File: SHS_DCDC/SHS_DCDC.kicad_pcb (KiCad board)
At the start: 6 copper layers, 100 x 100 mm, 130 parts, among them J1 Barrel_Jack, J2 USB_A, J3 Conn_ARM_JTAG_SWD_10, J4 Conn_01x02_Male, Q1 BSS84, Q10 PMV100XPEAR, Q11 PMV100XPEAR, Q12 PMV100XPEAR, Q13 PMV100XPEAR, Q14 PMV100XPEAR, Q15 BSS84, Q16 PMV100XPEAR, Q17 PMV100XPEAR, Q18 BSS84, Q19 2N7002, Q2 PMV100XPEAR, Q20 BSS84, Q21 2N7002, Q3 2N7002, Q4 2N7002, Q5 PMV100XPEAR, Q6 2N7002, Q7 PMV100XPEAR, Q8 Q_PMOS_DGS, Q9 PMV100XPEAR, U1 RT8299-WDFN10L, U2 INA181, U3 LMV324AIDR, U4 LMV358IDR, U5 MP3414A, U6 ESP32-S2-MINI-1, U7 MCP101, U8 MIC5501-3.0YM5, U9 BD49LxxG, Y1 2-SMD no lead

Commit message: 3D rendering progress
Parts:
- removed S1: TS02-66-70-BK-160-LCR-D, Library:SW_TS02-66-70-BK-160-LCR-D
- added SW1: TACT_SW, SHS_DCDC:ESWITCH_TL1105, B.Cu at (7.60, 58.9)
- J1, J2: moved to B.Cu
- L2: value L -> 1.5 uH
- moved C26 8.01 mm to (83.5, 19.4), turned to 0 degrees
- moved C27 8.00 mm to (83.5, 15.8), turned to 0 degrees
- moved J2 5.00 mm to (85.0, 12.0), turned to 0 degrees
- turned J1 to -90 degrees
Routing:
- net Net-(L2-Pad1): track 9.46 -> 0.00 mm
- net USB_D-: track 99.9 -> 107.8 mm
- net Net-(C26-Pad2): track 60.0 -> 55.8 mm
- net USB_D+: track 97.2 -> 98.9 mm

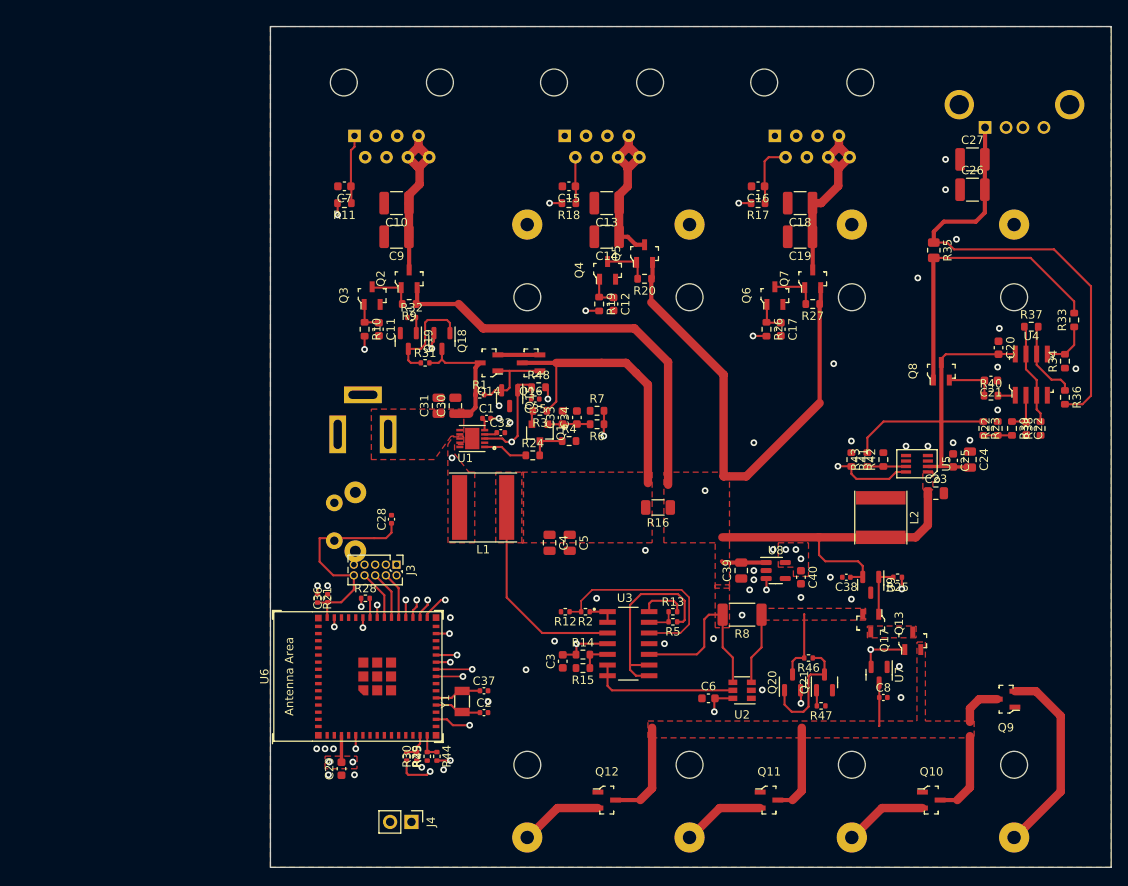
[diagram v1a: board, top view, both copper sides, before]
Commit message: 3D missing part
Many parts with no 3D view, have completed all of them
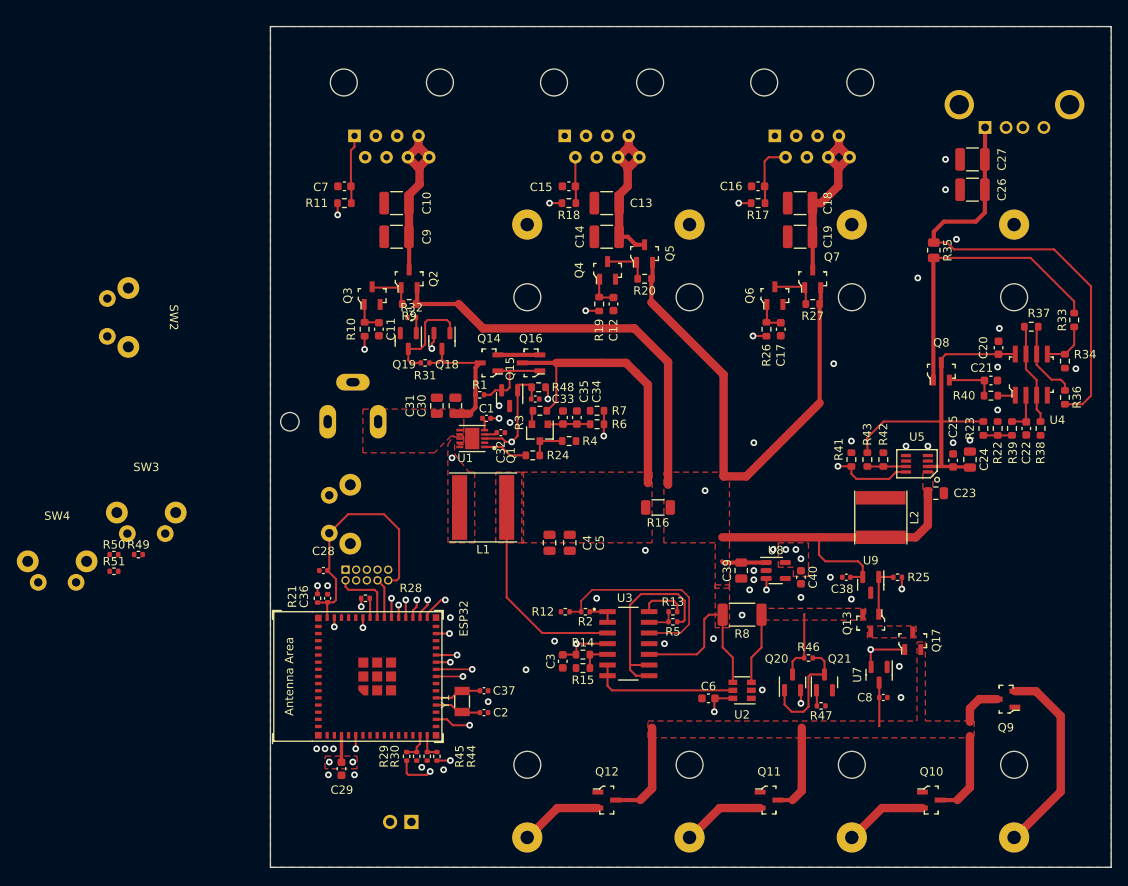
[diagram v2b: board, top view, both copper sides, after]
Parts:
- added R49: 10k, Resistor_SMD:R_0402_1005Metric, F.Cu at (-15.7, 62.8)
- added R50: 10k, Resistor_SMD:R_0402_1005Metric, F.Cu at (-18.6, 62.8)
- added R51: 10k, Resistor_SMD:R_0402_1005Metric, F.Cu at (-18.6, 64.8)
- added SW2: TACT_SW, SHS_DCDC:ESWITCH_TL1105, F.Cu at (-19.4, 34.6)
- added SW3: TACT_SW, SHS_DCDC:ESWITCH_TL1105, F.Cu at (-14.8, 60.3)
- added SW4: TACT_SW, SHS_DCDC:ESWITCH_TL1105, F.Cu at (-25.4, 66.1)
- J1: value Barrel_Jack -> PJ-059A; footprint digikey-footprints:Barrel_Jack_5.5mmODx2.1mmID_PJ-202A -> SHS_DCDC:CUI_PJ-059A
- J3, J4: moved to B.Cu
- moved C28 10.1 mm to (6.30, 64.7), turned to 180 degrees
- moved J3 6.10 mm to (8.93, 64.6)
- moved J1 2.35 mm to (12.8, 47.0), turned to 180 degrees
- moved SW1 1.08 mm to (7.00, 58.0)
- moved C31 0.20 mm to (19.8, 45.1)
- turned J4 to 90 degrees
- renumbered U6 to ESP32
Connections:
- J1 pad 3: (no net) -> GND
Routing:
- net MCU_TL_ONOFFSIG: track 71.7 -> 14.1 mm
- net V_MCU: track 115.2 -> 83.4 mm
- net MCU_RST: track 26.0 -> 29.8 mm
- net MCU_MTCK: track 5.66 -> 7.76 mm, vias 0 -> 1
- net MCU_MTMS: track 5.98 -> 7.81 mm, vias 1 -> 0
- net MCU_MTDI: track 6.01 -> 4.77 mm
- net MCU_MTDO: track 5.83 -> 6.11 mm, vias 0 -> 1

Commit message: ESP32 cornering
Moving the ESP32 on the bottom corner of the board
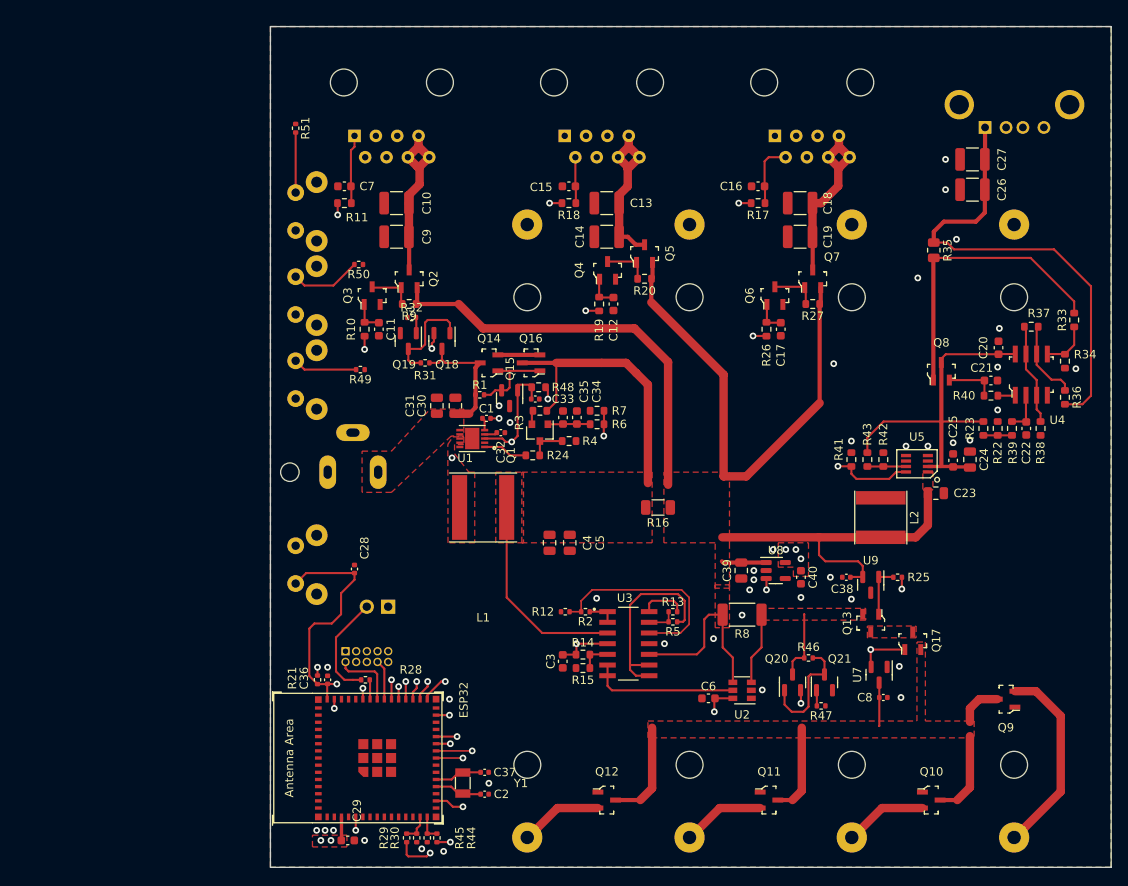
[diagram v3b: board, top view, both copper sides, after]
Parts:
- SW2, SW3, SW4: moved to B.Cu
- moved R51 57.0 mm to (3.00, 12.1), turned to -90 degrees
- moved SW4 52.4 mm to (3.00, 22.0), turned to 90 degrees
- moved R50 45.1 mm to (10.5, 28.3), turned to 180 degrees
- moved R49 34.4 mm to (10.7, 40.8), turned to 180 degrees
- moved SW3 33.4 mm to (3.00, 32.0), turned to 90 degrees
- moved J4 25.7 mm to (14.0, 69.0)
- moved SW2 23.6 mm to (3.00, 42.0), turned to 90 degrees
- moved C2 9.70 mm to (25.5, 91.3)
- moved C37 9.70 mm to (25.5, 88.7)
- moved Y1 9.70 mm to (22.9, 90.0)
- moved C36 9.70 mm to (6.80, 77.7)
- moved ESP32 9.70 mm to (12.7, 87.0)
- moved J3 9.70 mm to (8.93, 74.3)
- moved R21 9.70 mm to (5.60, 77.7)
- moved R28 9.70 mm to (11.3, 77.7)
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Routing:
- net MCU_5V_EN: track 70.4 -> 24.7 mm
- net MCU_BL1_ONOFFSIG: track 74.5 -> 57.3 mm
- net MCU_TX: track 28.5 -> 12.6 mm, vias 1 -> 0
- net USB_D-: track 107.8 -> 118.9 mm
- net MCU_RX: track 26.7 -> 17.0 mm
- net MCU_PWM_BL2: track 70.8 -> 80.5 mm
- net Net-(Q18-Pad2): track 57.0 -> 66.7 mm
- net MCU_PWM_TL: track 35.4 -> 45.1 mm
- net MCU_PWM_BL1: track 53.9 -> 63.6 mm
- net MCU_CTRL_B2: track 0.00 -> 8.46 mm
- net MCU_BL2_ONOFFSIG: track 89.1 -> 97.2 mm
- net MCU_CTRL_B1: track 0.00 -> 7.62 mm
- net USB_D+: track 98.9 -> 106.2 mm
- net MCU_CTRL_B3: track 0.00 -> 7.15 mm
- net MCU_RST: track 29.8 -> 35.9 mm, vias 0 -> 1
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- added copper zone on B.Cu, net GND

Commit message: DFU update
PCB update to setup 3 ways of FW/Debug capability:
1. JTAG (FW & Debug)
2. USB DFU (FW & Debug)
3. UART (FW only)
With BOOT0 button installed too
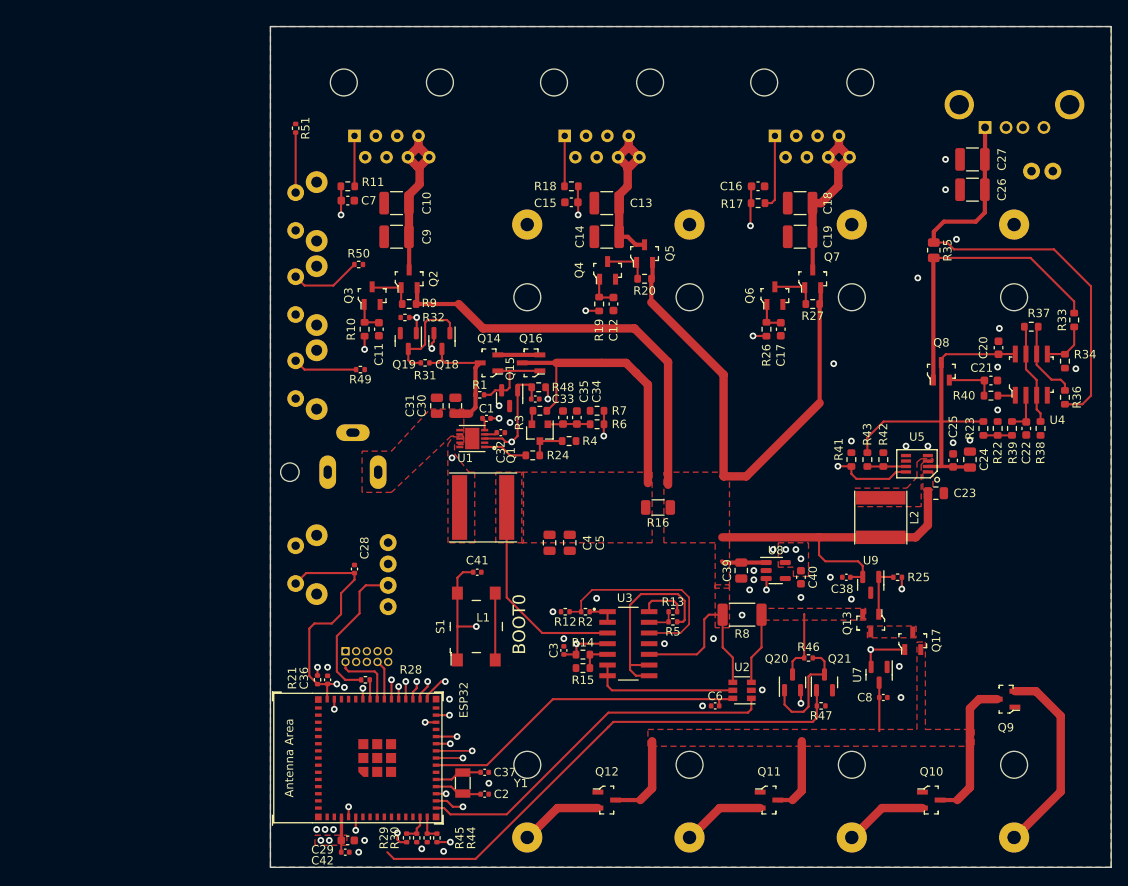
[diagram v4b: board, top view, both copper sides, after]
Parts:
- added C41: 100nF, Capacitor_SMD:C_0402_1005Metric, F.Cu at (24.6, 64.9)
- added C42: 100nF, Capacitor_SMD:C_0402_1005Metric, F.Cu at (8.90, 98.2)
- added J5: 640456-2, digikey-footprints:PinHeader_1x2_P2.54mm_Drill1.02mm, B.Cu at (93.1, 17.2)
- added S1: PTS645SM43SMTR92_LFS, digikey-footprints:Switch_Tactile_SMD_6x6mm_PTS645, F.Cu at (24.5, 71.4)
- C29: value 10uF -> 22uF
- C3, C6: footprint Capacitor_SMD:C_0603_1608Metric -> Capacitor_SMD:C_0402_1005Metric
- J4: value Conn_01x02_Male -> 0022232041; footprint Connector_PinHeader_2.54mm:PinHeader_1x02_P2.54mm_Vertical -> digikey-kicad-library-master:PinHeader_1x4_P2.54mm_Drill1.02mm
- R11, R17, R18: value 100k -> 1k
- moved R11 2.04 mm to (9.20, 19.0)
- moved R18 2.02 mm to (35.8, 19.0), turned to 0 degrees
- moved C15 1.92 mm to (35.8, 20.9)
- moved C7 1.75 mm to (9.20, 20.7), turned to 0 degrees
- moved C3 1.31 mm to (34.9, 74.2), turned to -90 degrees
- moved C6 1.20 mm to (52.9, 80.8)
- moved R32 0.80 mm to (16.0, 34.6)
- turned C16 to 0 degrees
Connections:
- net LOAD_BULB1 renamed LOAD_L2
- net LOAD_BULB2 renamed LOAD_L3
- net LOAD_TL renamed LOAD_L1
- net MCU_PWM_BL1 renamed MCU_PWM_L2
- net MCU_PWM_BL2 renamed MCU_PWM_L3
- net MCU_PWM_TL renamed MCU_PWM_L1
- net OP_VS renamed MCU_ADC_IPV
- Bulb1 pad 1: unconnected-(Bulb1-Pad1) -> Net-(Bulb1-Pad1)
- Bulb1 pad 2: MCU_BL1_ONOFFSIG -> GND
- Bulb2 pad 1: unconnected-(Bulb2-Pad1) -> Net-(Bulb2-Pad1)
- Bulb2 pad 2: MCU_BL2_ONOFFSIG -> GND
- C15 pad 1: MCU_BL1_ONOFFSIG -> MCU_L2_ONOFFSIG
- C16 pad 1: MCU_BL2_ONOFFSIG -> MCU_L3_ONOFFSIG
- C3 pad 2: V_MCU -> MCU_LMV324_VDD
- C6 pad 2: V_MCU -> MCU_INA181_VDD
- C7 pad 1: MCU_TL_ONOFFSIG -> MCU_L1_ONOFFSIG
- ESP32 pad 16: unconnected-(ESP32-Pad16) -> MCU_ADC_IBAT
- ESP32 pad 18: unconnected-(ESP32-Pad18) -> MCU_LMV324_VDD
- ESP32 pad 22: unconnected-(ESP32-Pad22) -> MCU_INA181_VDD
- ESP32 pad 25: MCU_BL2_ONOFFSIG -> MCU_L3_ONOFFSIG
- ESP32 pad 26: MCU_BL1_ONOFFSIG -> MCU_L2_ONOFFSIG
- ESP32 pad 28: unconnected-(ESP32-Pad28) -> MCU_L1_ONOFFSIG
- ESP32 pad 4: unconnected-(ESP32-Pad4) -> Net-(ESP32-Pad4)
- ESP32 pad 44: MCU_TL_ONOFFSIG -> MCU_ADC_PV_CTRL
- ESP32 pad 9: unconnected-(ESP32-Pad9) -> MCU_ADC_BAT_CTRL
- R11 pad 1: MCU_TL_ONOFFSIG -> Net-(R11-Pad1)
- R11 pad 2: V_MCU -> MCU_L1_ONOFFSIG
- R14 pad 1: V_MCU -> MCU_LMV324_VDD
- R17 pad 1: MCU_BL2_ONOFFSIG -> Net-(Bulb2-Pad1)
- R17 pad 2: V_MCU -> MCU_L3_ONOFFSIG
- R18 pad 1: MCU_BL1_ONOFFSIG -> Net-(Bulb1-Pad1)
- R18 pad 2: V_MCU -> MCU_L2_ONOFFSIG
- TubeLight1 pad 1: MCU_TL_ONOFFSIG -> Net-(R11-Pad1)
- TubeLight1 pad 2: unconnected-(TubeLight1-Pad2) -> GND
- U2 pad 6: V_MCU -> MCU_INA181_VDD
- U3 pad 4: V_MCU -> MCU_LMV324_VDD
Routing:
- net MCU_BL2_ONOFFSIG: track 97.2 -> 0.00 mm, vias 1 -> 0
- net MCU_L3_ONOFFSIG: track 0.00 -> 84.4 mm, vias 0 -> 2
- net MCU_L1_ONOFFSIG: track 0.00 -> 78.9 mm, vias 0 -> 2
- net V_MCU: track 82.9 -> 5.12 mm, vias 11 -> 6
- net MCU_L2_ONOFFSIG: track 0.00 -> 74.8 mm, vias 0 -> 2
- net MCU_ADC_PV_CTRL: track 1.88 -> 63.9 mm, vias 0 -> 2
- net MCU_ADC_BAT_CTRL: track 1.88 -> 61.6 mm
- net MCU_BL1_ONOFFSIG: track 57.3 -> 0.00 mm, vias 1 -> 0
- net MCU_5V_EN: track 24.7 -> 76.4 mm
- net Net-(ESP32-Pad4): track 0.00 -> 45.2 mm, vias 0 -> 2
- net MCU_ADC_IBAT: track 0.00 -> 44.3 mm
- net MCU_INA181_VDD: track 0.00 -> 39.4 mm
- net MCU_LMV324_VDD: track 0.00 -> 32.3 mm, vias 0 -> 2
- net MCU_TL_ONOFFSIG: track 14.1 -> 0.00 mm, vias 1 -> 0
- net Net-(Bulb2-Pad1): track 0.00 -> 8.94 mm
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- added copper zone on In3.Cu, net GND
- added copper zone on F.Cu, net Net-(L2-Pad1)
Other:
- board text added: "1. 2. 3. 4."
- board text added: "BOOT0"
- board text added: "BULB1"
- board text added: "BULB2"
- board text added: "COMM/PROG LINES J4 1.GND 2.MCU_VDD 3.MCU_TX 4.MCU_RX"
- board text added: "JTAG"
- board text added: "RST"
- board text added: "TUBEL1"
- board text added: "USB_DFU"
